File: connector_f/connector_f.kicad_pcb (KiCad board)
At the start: 2 copper layers, 120 x 47.1 mm, 33 parts, among them J1 PowerOut, J2 PowerIn, J3 CANFD_In, U1 SKA2P1_TX, U2 TJA1042T, U3 SKA2P1_RX, U5 XC6206P182MR, U6 LSF0102DCUR

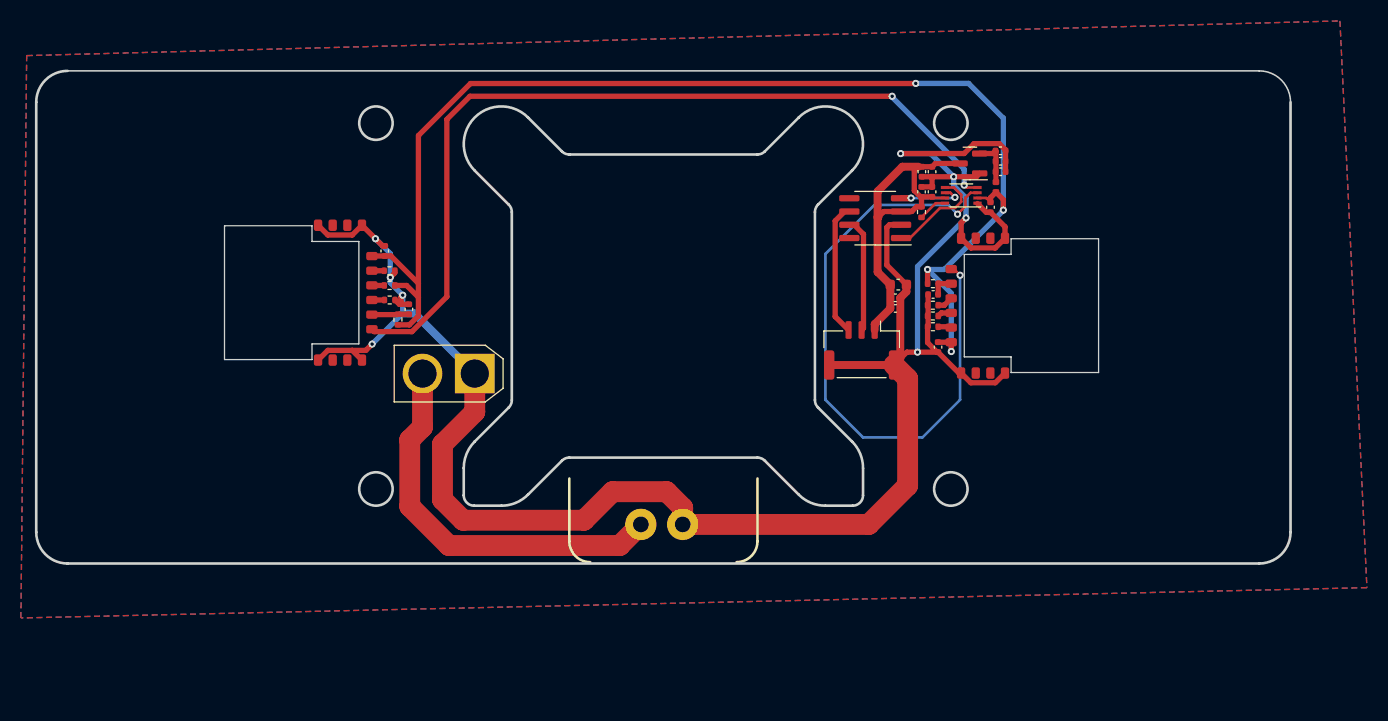
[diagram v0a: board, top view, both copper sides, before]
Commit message: [New] Add connector m
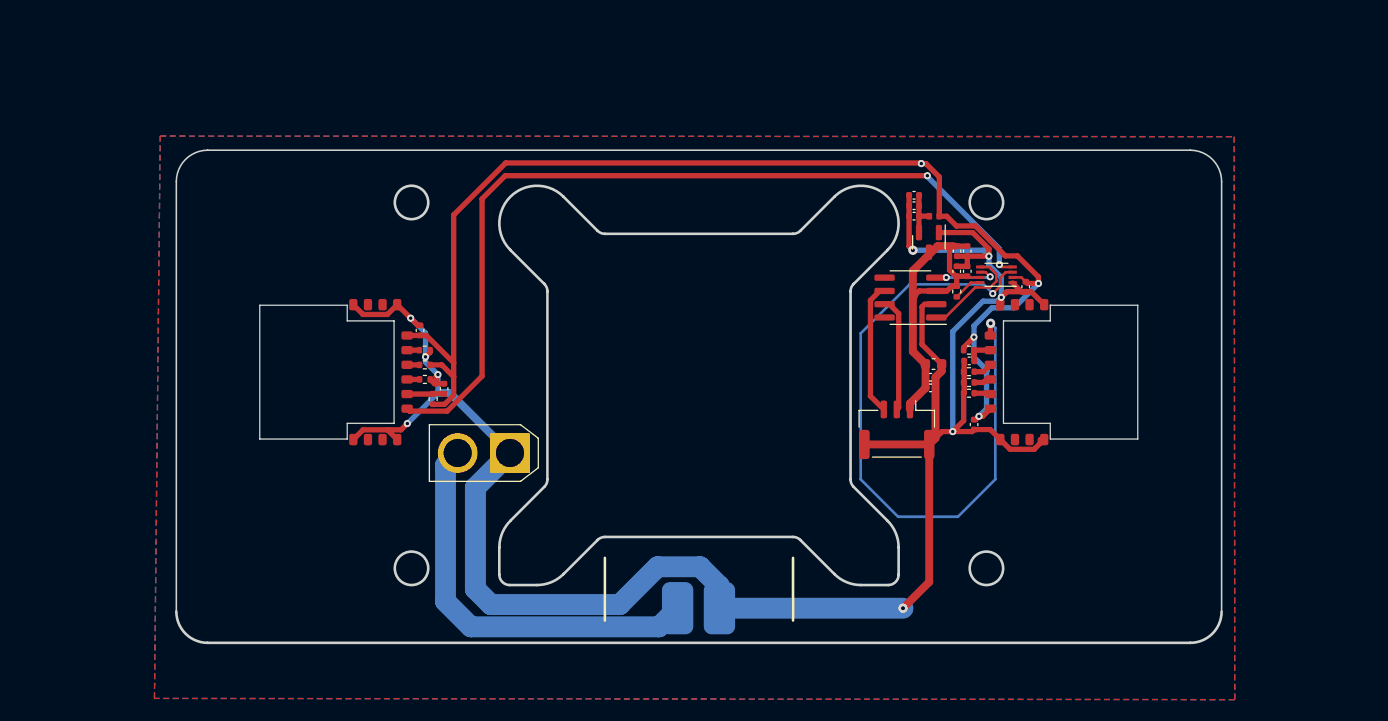
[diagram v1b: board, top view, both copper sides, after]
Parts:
- J1: footprint Rolling_Custom:POGOPIN-E21160-ASB-2PIN -> Rolling_Custom:POGOPIN-2PAD
- moved C17 10.4 mm to (125.6, 45.1), turned to 180 degrees
- moved C18 9.30 mm to (125.6, 44.1), turned to 180 degrees
- moved J1 8.76 mm to (105.0, 82.6), turned to 0 degrees
- moved C19 8.57 mm to (125.6, 43.1), turned to 180 degrees
- moved U5 8.51 mm to (127.0, 47.6), turned to -90 degrees
- moved C1 8.31 mm to (78.3, 56.0)
- moved C13 8.31 mm to (136.3, 51.8)
- moved C14 8.31 mm to (130.7, 48.4)
- moved C15 8.31 mm to (129.7, 48.4)
- moved C2 8.31 mm to (80.6, 61.6)
- moved C21 8.31 mm to (129.7, 50.4)
- moved C23 8.31 mm to (130.7, 50.4)
- moved C4 8.31 mm to (127.2, 61.5)
- moved C5 8.31 mm to (127.2, 60.5)
- moved R1 8.31 mm to (78.8, 57.9)
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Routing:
- net +1V8: track 122.5 -> 116.8 mm
- net GND: track 213.1 -> 209.4 mm, vias 8 -> 9
- net TX_1V8: track 61.0 -> 64.3 mm
- net +5V: track 34.6 -> 31.8 mm
- net +24V: track 37.7 -> 38.6 mm
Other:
- board size 120 x 47.1 mm -> 100 x 47.1 mm
